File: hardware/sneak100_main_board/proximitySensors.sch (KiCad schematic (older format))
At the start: 23 parts, among them Q3 SFH-313FA, Q4 SFH-313FA, Q5 SFH-313FA, Q6 SFH-313FA, U6 CD4051B, U7 CD4051B

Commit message: PCB first full layout
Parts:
- R10, R11, R12, R13, R14, R16, R7, R8, R9: footprint Resistor_SMD:R_0805_2012Metric -> Resistor_SMD:R_0603_1608Metric
- renumbered C14 to C15, C15 to C16, U6 to U7, U7 to U8
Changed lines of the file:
@@
 $EndDescr
 $Comp
-L Analog_Switch:CD4051B U6
+L Analog_Switch:CD4051B U7
 U 1 1 60E0E536
 P 3100 4800
-F 0 "U6" H 3500 5600 50  0000 C CNN
+F 0 "U7" H 3500 5600 50  0000 C CNN
 F 1 "CD4051B" H 3500 5500 50  0000 C CNN
 F 2 "Package_SO:SOIC-16_3.9x9.9mm_P1.27mm" H 3250 4050 50  0001 L CNN
@@
 $EndComp
 $Comp
-L Analog_Switch:CD4051B U7
+L Analog_Switch:CD4051B U8
 U 1 1 60E0F4C1
 P 7750 4800
-F 0 "U7" H 8200 5600 50  0000 C CNN
+F 0 "U8" H 8200 5600 50  0000 C CNN
 F 1 "CD4051B" H 8200 5500 50  0000 C CNN
 F 2 "Package_SO:SOIC-16_3.9x9.9mm_P1.27mm" H 7900 4050 50  0001 L CNN
@@
 ADD2
 $Comp
-L power:GND #PWR072
+L power:GND #PWR073
 U 1 1 60E1F519
 P 3100 5600
-F 0 "#PWR072" H 3100 5350 50  0001 C CNN
+F 0 "#PWR073" H 3100 5350 50  0001 C CNN
 F 1 "GND" H 3105 5427 50  0000 C CNN
 F 2 "" H 3100 5600 50  0001 C CNN
@@
 $EndComp
 $Comp
-L power:GND #PWR073
+L power:GND #PWR074
 U 1 1 60E212D3
 P 7750 5600
-F 0 "#PWR073" H 7750 5350 50  0001 C CNN
+F 0 "#PWR074" H 7750 5350 50  0001 C CNN
 F 1 "GND" H 7755 5427 50  0000 C CNN
 F 2 "" H 7750 5600 50  0001 C CNN
@@
 $EndComp
 $Comp
-L power:GND #PWR069
+L power:GND #PWR070
 U 1 1 60E218A7
 P 7200 4850
-F 0 "#PWR069" H 7200 4600 50  0001 C CNN
+F 0 "#PWR070" H 7200 4600 50  0001 C CNN
 F 1 "GND" H 7205 4677 50  0000 C CNN
 F 2 "" H 7200 4850 50  0001 C CNN
@@
 $EndComp
 $Comp
-L power:+3.3V #PWR064
+L power:+3.3V #PWR065
 U 1 1 60E248E2
 P 3200 4100
-F 0 "#PWR064" H 3200 3950 50  0001 C CNN
+F 0 "#PWR065" H 3200 3950 50  0001 C CNN
 F 1 "+3.3V" H 3215 4273 50  0000 C CNN
 F 2 "" H 3200 4100 50  0001 C CNN
@@
 $EndComp
 $Comp
-L power:+3.3V #PWR066
+L power:+3.3V #PWR067
 U 1 1 60E24FA6
 P 7850 4100
-F 0 "#PWR066" H 7850 3950 50  0001 C CNN
+F 0 "#PWR067" H 7850 3950 50  0001 C CNN
 F 1 "+3.3V" H 7865 4273 50  0000 C CNN
 F 2 "" H 7850 4100 50  0001 C CNN
@@
 $EndComp
 $Comp
-L power:+3.3V #PWR068
+L power:+3.3V #PWR069
 U 1 1 60E25559
 P 2000 4650
-F 0 "#PWR068" H 2000 4500 50  0001 C CNN
+F 0 "#PWR069" H 2000 4500 50  0001 C CNN
 F 1 "+3.3V" H 2015 4823 50  0000 C CNN
 F 2 "" H 2000 4650 50  0001 C CNN
@@
 F 0 "R16" H 2120 5046 50  0000 L CNN
 F 1 "4k7" H 2120 4955 50  0000 L CNN
-F 2 "Resistor_SMD:R_0805_2012Metric" V 1980 5000 50  0001 C CNN
+F 2 "Resistor_SMD:R_0603_1608Metric" V 1980 5000 50  0001 C CNN
 F 3 "~" H 2050 5000 50  0001 C CNN
 	1    2050 5000
@@
 $EndComp
 $Comp
-L power:GND #PWR071
+L power:GND #PWR072
 U 1 1 60E46C69
 P 2050 5150
-F 0 "#PWR071" H 2050 4900 50  0001 C CNN
+F 0 "#PWR072" H 2050 4900 50  0001 C CNN
 F 1 "GND" H 2055 4977 50  0000 C CNN
 F 2 "" H 2050 5150 50  0001 C CNN
@@
 IR led current resistor calculations:\n\ntarget current: I = 100mA\ninput voltage: U = 3.3V\nforward voltage: Uf = 1.7V\n\nR = (U-Uf)/I\nR = (3.3 - 1.7)/0.1 = 16ohm -> 20ohm
 $Comp
-L power:GND #PWR057
+L power:GND #PWR058
 U 1 1 60ED3093
 P 6000 3050
-F 0 "#PWR057" H 6000 2800 50  0001 C CNN
+F 0 "#PWR058" H 6000 2800 50  0001 C CNN
 F 1 "GND" H 6005 2877 50  0000 C CNN
 F 2 "" H 6000 3050 50  0001 C CNN
@@
 F 0 "R7" H 6070 2446 50  0000 L CNN
 F 1 "10k" H 6070 2355 50  0000 L CNN
-F 2 "Resistor_SMD:R_0805_2012Metric" V 5930 2400 50  0001 C CNN
+F 2 "Resistor_SMD:R_0603_1608Metric" V 5930 2400 50  0001 C CNN
 F 3 "~" H 6000 2400 50  0001 C CNN
 	1    6000 2400
@@
 $EndComp
 $Comp
-L power:+3.3V #PWR049
+L power:+3.3V #PWR050
 U 1 1 60ED4A76
 P 6000 2250
-F 0 "#PWR049" H 6000 2100 50  0001 C CNN
+F 0 "#PWR050" H 6000 2100 50  0001 C CNN
 F 1 "+3.3V" H 6015 2423 50  0000 C CNN
 F 2 "" H 6000 2250 50  0001 C CNN
@@
 RX_IN1
 $Comp
-L power:GND #PWR053
+L power:GND #PWR054
 U 1 1 60EE410D
 P 1550 3050
-F 0 "#PWR053" H 1550 2800 50  0001 C CNN
+F 0 "#PWR054" H 1550 2800 50  0001 C CNN
 F 1 "GND" H 1555 2877 50  0000 C CNN
 F 2 "" H 1550 3050 50  0001 C CNN
@@
 F 0 "R11" H 1620 2646 50  0000 L CNN
 F 1 "20" H 1620 2555 50  0000 L CNN
-F 2 "Resistor_SMD:R_0805_2012Metric" V 1480 2600 50  0001 C CNN
+F 2 "Resistor_SMD:R_0603_1608Metric" V 1480 2600 50  0001 C CNN
 F 3 "~" H 1550 2600 50  0001 C CNN
 	1    1550 2600
@@
 TX_OUT1
 $Comp
-L power:GND #PWR054
+L power:GND #PWR055
 U 1 1 60EF4EEA
 P 2100 3050
-F 0 "#PWR054" H 2100 2800 50  0001 C CNN
+F 0 "#PWR055" H 2100 2800 50  0001 C CNN
 F 1 "GND" H 2105 2877 50  0000 C CNN
 F 2 "" H 2100 3050 50  0001 C CNN
@@
 F 0 "R12" H 2170 2646 50  0000 L CNN
 F 1 "20" H 2170 2555 50  0000 L CNN
-F 2 "Resistor_SMD:R_0805_2012Metric" V 2030 2600 50  0001 C CNN
+F 2 "Resistor_SMD:R_0603_1608Metric" V 2030 2600 50  0001 C CNN
 F 3 "~" H 2100 2600 50  0001 C CNN
 	1    2100 2600
@@
 TX_OUT2
 $Comp
-L power:GND #PWR055
+L power:GND #PWR056
 U 1 1 60EF5BFB
 P 2650 3050
-F 0 "#PWR055" H 2650 2800 50  0001 C CNN
+F 0 "#PWR056" H 2650 2800 50  0001 C CNN
 F 1 "GND" H 2655 2877 50  0000 C CNN
 F 2 "" H 2650 3050 50  0001 C CNN
@@
 F 0 "R13" H 2720 2646 50  0000 L CNN
 F 1 "20" H 2720 2555 50  0000 L CNN
-F 2 "Resistor_SMD:R_0805_2012Metric" V 2580 2600 50  0001 C CNN
+F 2 "Resistor_SMD:R_0603_1608Metric" V 2580 2600 50  0001 C CNN
 F 3 "~" H 2650 2600 50  0001 C CNN
 	1    2650 2600
@@
 TX_OUT3
 $Comp
-L power:GND #PWR056
+L power:GND #PWR057
 U 1 1 60EF6854
 P 3200 3050
-F 0 "#PWR056" H 3200 2800 50  0001 C CNN
+F 0 "#PWR057" H 3200 2800 50  0001 C CNN
 F 1 "GND" H 3205 2877 50  0000 C CNN
 F 2 "" H 3200 3050 50  0001 C CNN
@@
 F 0 "R14" H 3270 2646 50  0000 L CNN
 F 1 "20" H 3270 2555 50  0000 L CNN
-F 2 "Resistor_SMD:R_0805_2012Metric" V 3130 2600 50  0001 C CNN
+F 2 "Resistor_SMD:R_0603_1608Metric" V 3130 2600 50  0001 C CNN
 F 3 "~" H 3200 2600 50  0001 C CNN
 	1    3200 2600
@@
 TX_OUT4
 $Comp
-L Device:C C15
+L Device:C C16
 U 1 1 60F1A0B6
 P 3950 3950
-F 0 "C15" H 4065 3996 50  0000 L CNN
+F 0 "C16" H 4065 3996 50  0000 L CNN
 F 1 "100nF" H 4065 3905 50  0000 L CNN
 F 2 "Capacitor_SMD:C_0603_1608Metric" H 3988 3800 50  0001 C CNN
@@
 $EndComp
 $Comp
-L power:+3.3V #PWR062
+L power:+3.3V #PWR063
 U 1 1 60F1B962
 P 3950 3800
-F 0 "#PWR062" H 3950 3650 50  0001 C CNN
+F 0 "#PWR063" H 3950 3650 50  0001 C CNN
 F 1 "+3.3V" H 3965 3973 50  0000 C CNN
 F 2 "" H 3950 3800 50  0001 C CNN
@@
 $EndComp
 $Comp
-L power:GND #PWR065
+L power:GND #PWR066
 U 1 1 60F1BF31
 P 3950 4100
-F 0 "#PWR065" H 3950 3850 50  0001 C CNN
+F 0 "#PWR066" H 3950 3850 50  0001 C CNN
 F 1 "GND" H 3955 3927 50  0000 C CNN
 F 2 "" H 3950 4100 50  0001 C CNN
@@
 $EndComp
 $Comp
-L Device:C C14
+L Device:C C15
 U 1 1 60F1EDF8
 P 8550 3900
-F 0 "C14" H 8665 3946 50  0000 L CNN
+F 0 "C15" H 8665 3946 50  0000 L CNN
 F 1 "100nF" H 8665 3855 50  0000 L CNN
 F 2 "Capacitor_SMD:C_0603_1608Metric" H 8588 3750 50  0001 C CNN
@@
 $EndComp
 $Comp
-L power:+3.3V #PWR061
+L power:+3.3V #PWR062
 U 1 1 60F1EDFE
 P 8550 3750
-F 0 "#PWR061" H 8550 3600 50  0001 C CNN
+F 0 "#PWR062" H 8550 3600 50  0001 C CNN
 F 1 "+3.3V" H 8565 3923 50  0000 C CNN
 F 2 "" H 8550 3750 50  0001 C CNN
@@
 $EndComp
 $Comp
-L power:GND #PWR063
+L power:GND #PWR064
 U 1 1 60F1EE04
 P 8550 4050
-F 0 "#PWR063" H 8550 3800 50  0001 C CNN
+F 0 "#PWR064" H 8550 3800 50  0001 C CNN
 F 1 "GND" H 8555 3877 50  0000 C CNN
 F 2 "" H 8550 4050 50  0001 C CNN
@@
 $EndComp
 $Comp
-L power:GND #PWR058
+L power:GND #PWR059
 U 1 1 60F34699
 P 6750 3050
-F 0 "#PWR058" H 6750 2800 50  0001 C CNN
+F 0 "#PWR059" H 6750 2800 50  0001 C CNN
 F 1 "GND" H 6755 2877 50  0000 C CNN
 F 2 "" H 6750 3050 50  0001 C CNN
@@
 F 0 "R8" H 6820 2446 50  0000 L CNN
 F 1 "10k" H 6820 2355 50  0000 L CNN
-F 2 "Resistor_SMD:R_0805_2012Metric" V 6680 2400 50  0001 C CNN
+F 2 "Resistor_SMD:R_0603_1608Metric" V 6680 2400 50  0001 C CNN
 F 3 "~" H 6750 2400 50  0001 C CNN
 	1    6750 2400
@@
 $EndComp
 $Comp
-L power:+3.3V #PWR050
+L power:+3.3V #PWR051
 U 1 1 60F346A5
 P 6750 2250
-F 0 "#PWR050" H 6750 2100 50  0001 C CNN
+F 0 "#PWR051" H 6750 2100 50  0001 C CNN
 F 1 "+3.3V" H 6765 2423 50  0000 C CNN
 F 2 "" H 6750 2250 50  0001 C CNN
@@
 RX_IN2
 $Comp
-L power:GND #PWR059
+L power:GND #PWR060
 U 1 1 60F35A4C
 P 7500 3050
-F 0 "#PWR059" H 7500 2800 50  0001 C CNN
+F 0 "#PWR060" H 7500 2800 50  0001 C CNN
 F 1 "GND" H 7505 2877 50  0000 C CNN
 F 2 "" H 7500 3050 50  0001 C CNN
@@
 F 0 "R9" H 7570 2446 50  0000 L CNN
 F 1 "10k" H 7570 2355 50  0000 L CNN
-F 2 "Resistor_SMD:R_0805_2012Metric" V 7430 2400 50  0001 C CNN
+F 2 "Resistor_SMD:R_0603_1608Metric" V 7430 2400 50  0001 C CNN
 F 3 "~" H 7500 2400 50  0001 C CNN
 	1    7500 2400
@@
 $EndComp
 $Comp
-L power:+3.3V #PWR051
+L power:+3.3V #PWR052
 U 1 1 60F35A58
 P 7500 2250
-F 0 "#PWR051" H 7500 2100 50  0001 C CNN
+F 0 "#PWR052" H 7500 2100 50  0001 C CNN
 F 1 "+3.3V" H 7515 2423 50  0000 C CNN
 F 2 "" H 7500 2250 50  0001 C CNN
@@
 RX_IN3
 $Comp
-L power:GND #PWR060
+L power:GND #PWR061
 U 1 1 60F38E59
 P 8250 3050
-F 0 "#PWR060" H 8250 2800 50  0001 C CNN
+F 0 "#PWR061" H 8250 2800 50  0001 C CNN
 F 1 "GND" H 8255 2877 50  0000 C CNN
 F 2 "" H 8250 3050 50  0001 C CNN
@@
 F 0 "R10" H 8320 2446 50  0000 L CNN
 F 1 "10k" H 8320 2355 50  0000 L CNN
-F 2 "Resistor_SMD:R_0805_2012Metric" V 8180 2400 50  0001 C CNN
+F 2 "Resistor_SMD:R_0603_1608Metric" V 8180 2400 50  0001 C CNN
 F 3 "~" H 8250 2400 50  0001 C CNN
 	1    8250 2400
@@
 $EndComp
 $Comp
-L power:+3.3V #PWR052
+L power:+3.3V #PWR053
 U 1 1 60F38E65
 P 8250 2250
-F 0 "#PWR052" H 8250 2100 50  0001 C CNN
+F 0 "#PWR053" H 8250 2100 50  0001 C CNN
 F 1 "+3.3V" H 8265 2423 50  0000 C CNN
 F 2 "" H 8250 2250 50  0001 C CNN
@@
 $EndComp
 $Comp
-L power:GND #PWR070
+L power:GND #PWR071
 U 1 1 60EAB75A
 P 5750 4950
-F 0 "#PWR070" H 5750 4700 50  0001 C CNN
+F 0 "#PWR071" H 5750 4700 50  0001 C CNN
 F 1 "GND" H 5755 4777 50  0000 C CNN
 F 2 "" H 5750 4950 50  0001 C CNN
@@
 	5750 4600 5750 4650
 $Comp
-L power:+3.3V #PWR067
+L power:+3.3V #PWR068
 U 1 1 60EC949D
 P 5750 4250
-F 0 "#PWR067" H 5750 4100 50  0001 C CNN
+F 0 "#PWR068" H 5750 4100 50  0001 C CNN
 F 1 "+3.3V" H 5765 4423 50  0000 C CNN
 F 2 "" H 5750 4250 50  0001 C CNN

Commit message: bluetooth en & status connection
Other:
- note added: "układ testowy, wymagane dalsze próby"
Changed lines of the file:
@@
 	1    0    0    -1
 $EndComp
+Text Notes 5100 3950 0    50   ~ 0
+układ testowy, wymagane dalsze próby
 $EndSCHEMATC

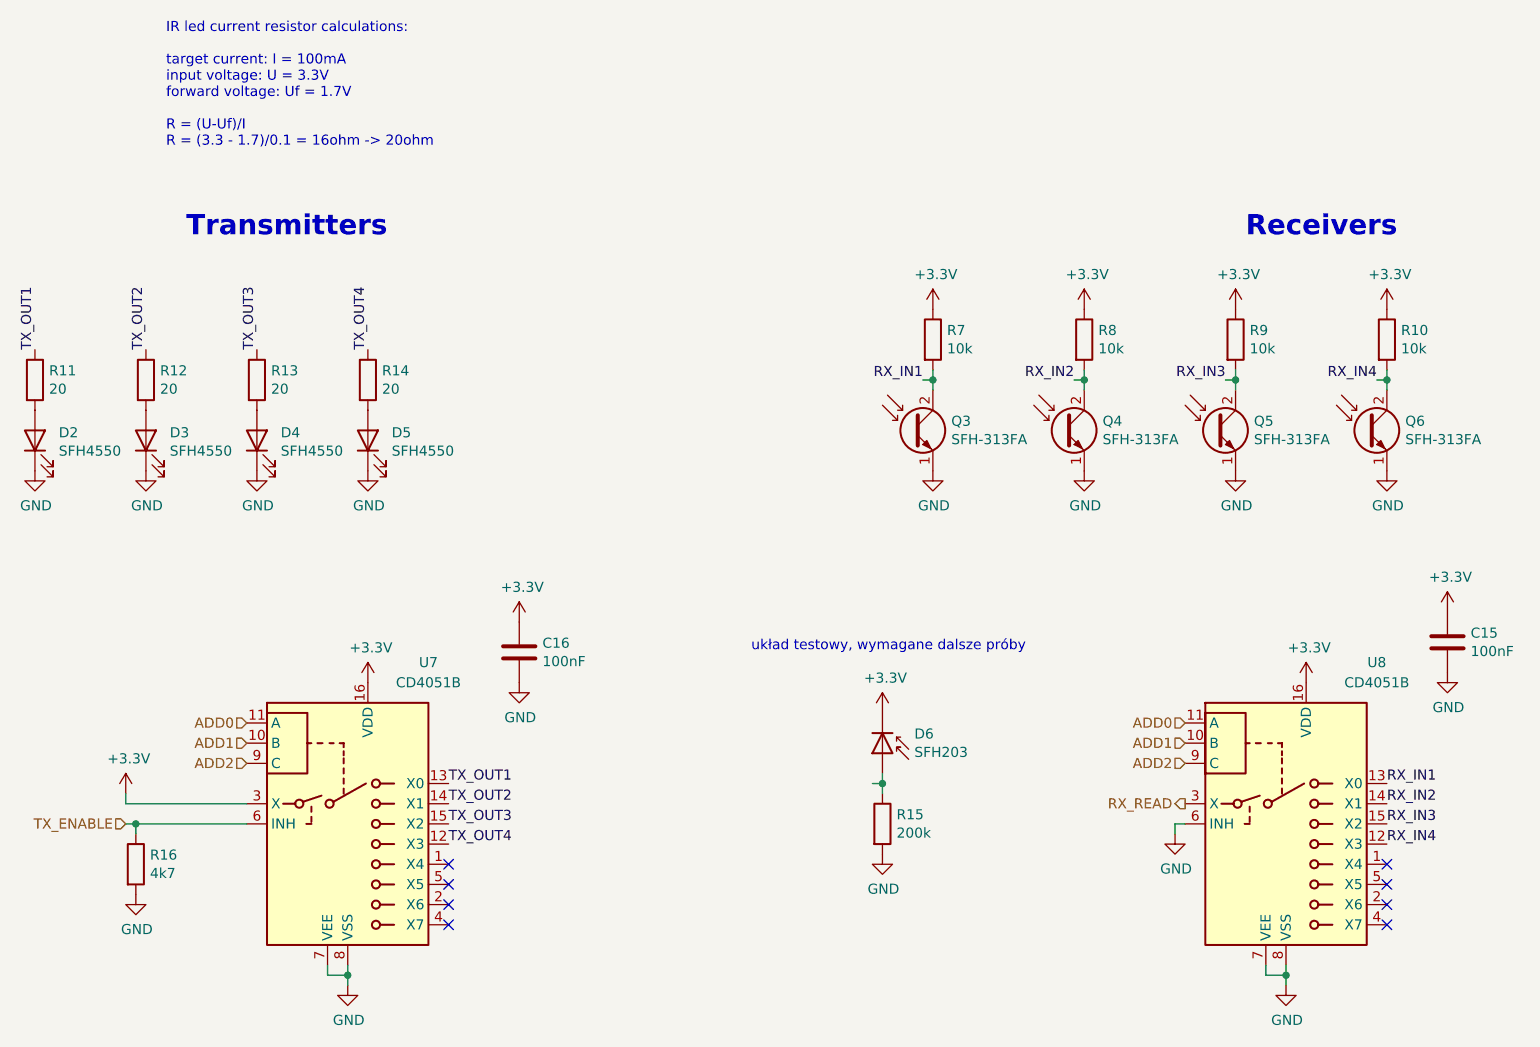
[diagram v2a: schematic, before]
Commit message: Add external proximity sensor, erase old from schematic
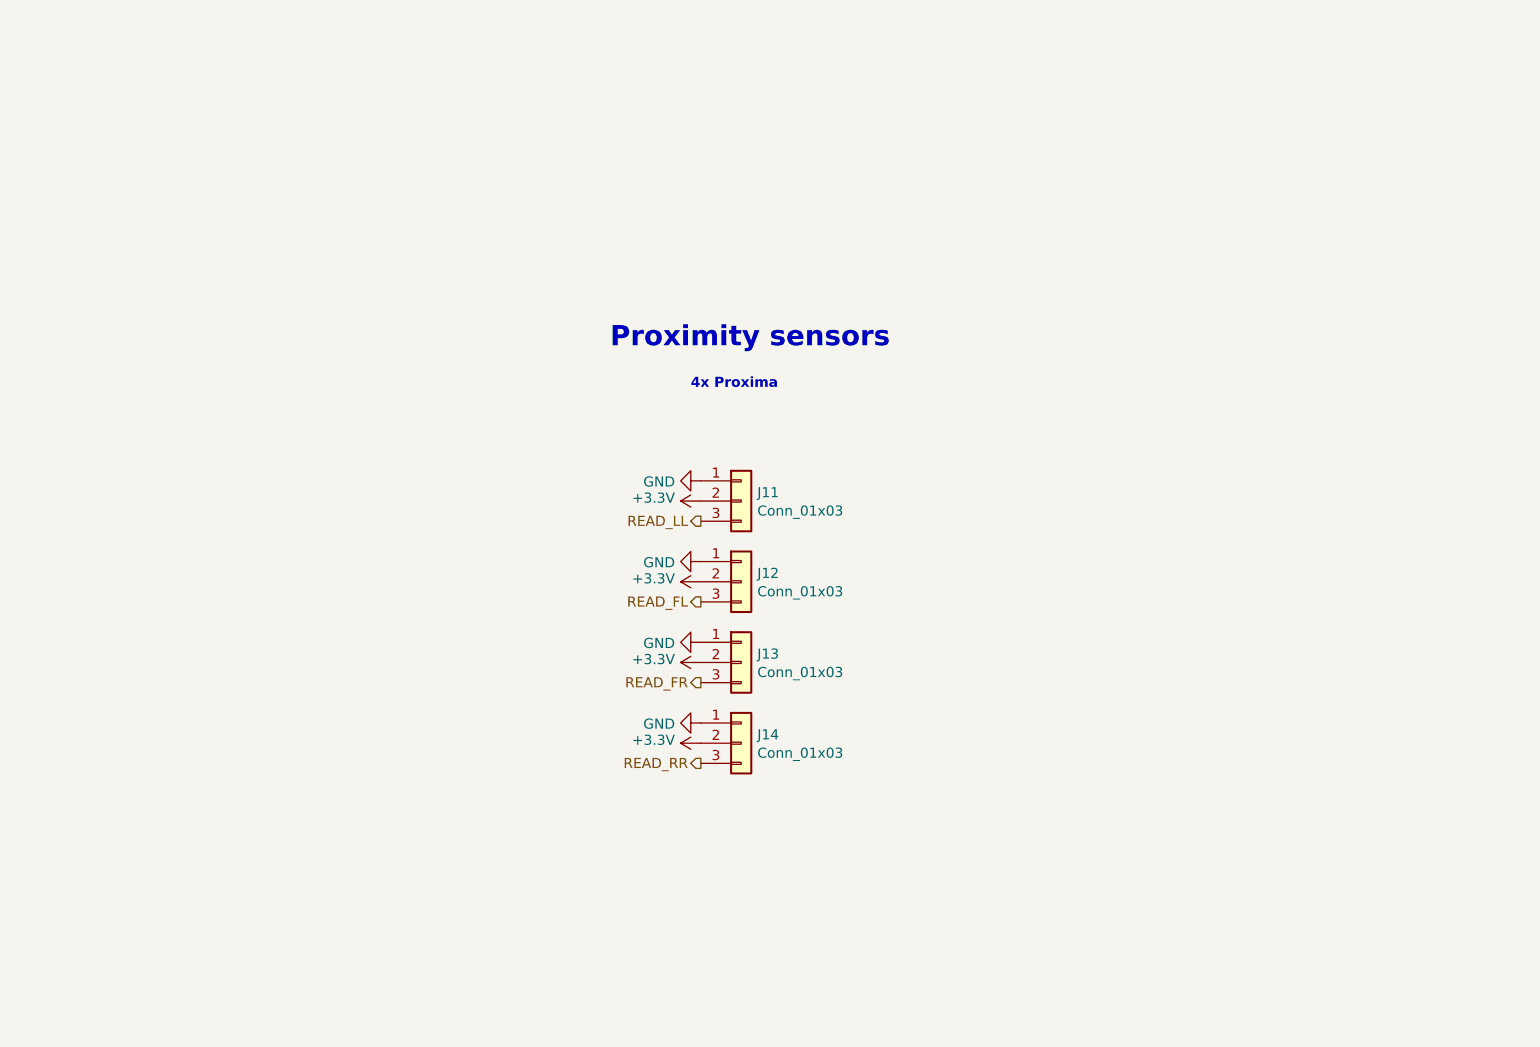
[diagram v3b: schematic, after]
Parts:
- removed C15, C16: 100nF, Capacitor_SMD:C_0603_1608Metric, symbol Device:C
- removed D2, D3, D4, D5: SFH4550, Connector_PinHeader_2.54mm:PinHeader_1x02_P2.54mm_Vertical, symbol Device:LED
- removed D6: SFH203, symbol Device:D_Photo
- removed Q3, Q4, Q5, Q6: SFH-313FA, Connector_PinHeader_2.54mm:PinHeader_1x02_P2.54mm_Vertical, symbol Device:Q_Photo_NPN_EC
- removed R10, R7, R8, R9: 10k, Resistor_SMD:R_0603_1608Metric, symbol Device:R
- removed R11, R12, R13, R14: 20, Resistor_SMD:R_0603_1608Metric, symbol Device:R
- removed R15: 200k, symbol Device:R
- removed R16: 4k7, Resistor_SMD:R_0603_1608Metric, symbol Device:R
- removed U7, U8: CD4051B, Package_SO:SOIC-16_3.9x9.9mm_P1.27mm, symbol Analog_Switch:CD4051B
- added J11, J12, J13, J14: Conn_01x03, Connector_PinHeader_2.54mm:PinHeader_1x03_P2.54mm_Vertical, symbol Connector_Generic:Conn_01x03
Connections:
- net labels added: READ_FL, READ_FR, READ_LL, READ_RR
- net labels removed: ADD0, ADD1, ADD2, RX_IN1, RX_IN2, RX_IN3, RX_IN4, RX_READ, TX_ENABLE, TX_OUT1, TX_OUT2, TX_OUT3, TX_OUT4
- wire segments 30 -> 0
- no-connect marks 8 -> 0
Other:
- note added: "4x Proxima"
- note added: "Proximity sensors"
- note removed: "IR led current resistor calculations:\n\ntarget current: I = 100mA\ninput voltage: U = 3.3V\nforward voltage: Uf = 1.7V\n\nR = (U-Uf)/I\nR = (3.3 - 1.7)/0.1 = 16ohm -> 20ohm"
- note removed: "Receivers"
- note removed: "Transmitters"
- note removed: "układ testowy, wymagane dalsze próby"
